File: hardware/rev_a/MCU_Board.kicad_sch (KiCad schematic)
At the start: 35 parts, among them J1 ST-Link, J2 Conn_01x08, J3 Bus, J4 Conn_01x08, J5 Conn_02x07_Odd_Even, SW1 nRST, U2 MC34063AD, U3 SN65HVD230, U5 STM32F042K6Tx, Y1 8Mhz

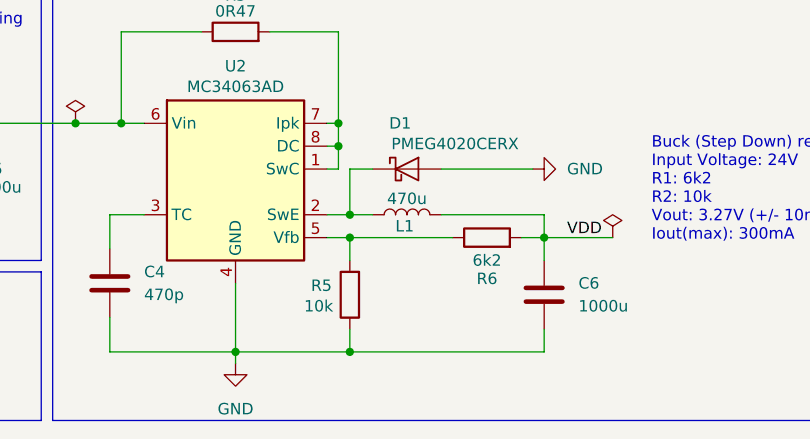
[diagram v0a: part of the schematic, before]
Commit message: Fix resistor value around DC/DC converter
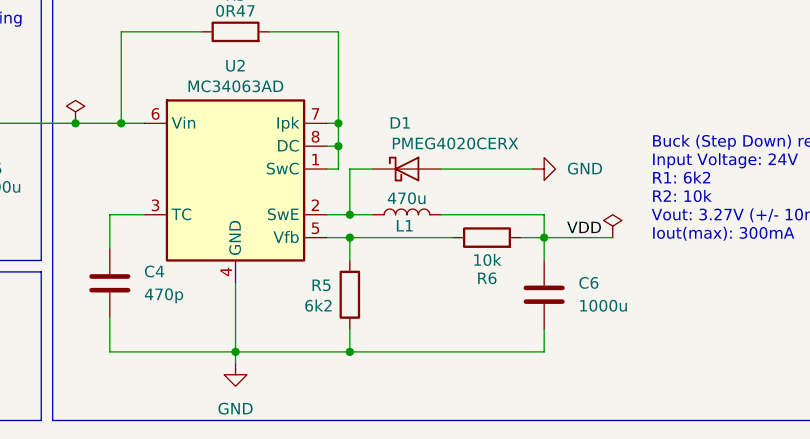
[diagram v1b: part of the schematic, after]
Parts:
- R5: value 10k -> 6k2
- R6: value 6k2 -> 10k
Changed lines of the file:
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@@
 			)
 		)
-		(property "Value" "10k"
+		(property "Value" "6k2"
 			(at 179.07 147.32 0)
 			(effects
@@
 			)
 		)
-		(property "Datasheet" "https://fr.farnell.com/multicomp/mcsr08x103-jtl/res-ceramique-10k-5-0-125w-0805/dp/2074340"
+		(property "Datasheet" "https://fr.farnell.com/multicomp/mcwr08x6201ftl/resistance-thick-film-6-2kohm/dp/2447709"
 			(at 184.15 146.05 0)
 			(effects
@@
 			)
 		)
-		(property "Value" "6k2"
+		(property "Value" "10k"
 			(at 199.39 142.24 90)
 			(effects
@@
 			)
 		)
-		(property "Datasheet" "https://fr.farnell.com/multicomp/mcwr08x6201ftl/resistance-thick-film-6-2kohm/dp/2447709"
+		(property "Datasheet" "https://fr.farnell.com/multicomp/mcsr08x103-jtl/res-ceramique-10k-5-0-125w-0805/dp/2074340"
 			(at 199.39 139.7 0)
 			(effects

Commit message: Version under review by PCBWay (Nucleo Shield)
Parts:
- removed C2: 18p, Capacitor_SMD:C_0805_2012Metric_Pad1.18x1.45mm_HandSolder, symbol Device:C
- removed C3, C7, C8, C9: 100n, Capacitor_SMD:C_0805_2012Metric_Pad1.18x1.45mm_HandSolder, symbol Device:C
- removed FB1: FerriteBead, Inductor_SMD:L_0805_2012Metric_Pad1.05x1.20mm_HandSolder, symbol Device:FerriteBead
- removed J1: ST-Link, custom:st-link, symbol Connector_Generic:Conn_01x04
- removed J2, J4: Conn_01x08, custom:CONN_01x08, symbol Connector_Generic:Conn_01x08
- removed J5: Conn_02x07_Odd_Even, custom:addr_jumpers, symbol Connector_Generic:Conn_02x07_Odd_Even
- removed R1: 100k, Resistor_SMD:R_0805_2012Metric_Pad1.20x1.40mm_HandSolder, symbol Device:R
- removed SW1: nRST, Button_Switch_SMD:SW_SPST_B3U-1000P-B, symbol Switch:SW_Push
- removed U5: STM32F042K6Tx, Package_QFP:LQFP-32_7x7mm_P0.8mm, symbol MCU_ST_STM32F0:STM32F042K6Tx
- removed Y1: 8Mhz, Crystal:Crystal_HC18-U_Vertical, symbol Device:Crystal_Small
- added J1, J5, J6, J7: Conn_01x15, Connector_PinHeader_2.54mm:PinHeader_1x15_P2.54mm_Vertical, symbol Connector_Generic:Conn_01x15
- added J2: Conn_01x02, Connector_PinHeader_2.54mm:PinHeader_1x02_P2.54mm_Vertical, symbol Connector_Generic:Conn_01x02
- C1: value 18p -> 100n; footprint Capacitor_SMD:C_0805_2012Metric_Pad1.18x1.45mm_HandSolder -> Capacitor_THT:C_Disc_D5.0mm_W2.5mm_P5.00mm
- C10: footprint Capacitor_SMD:C_0805_2012Metric_Pad1.18x1.45mm_HandSolder -> Capacitor_THT:C_Disc_D5.0mm_W2.5mm_P5.00mm
- C4: value 470p -> 680p; footprint Capacitor_SMD:C_0805_2012Metric_Pad1.18x1.45mm_HandSolder -> Capacitor_THT:C_Disc_D5.0mm_W2.5mm_P5.00mm
- R2, R4, R5, R6: footprint Resistor_SMD:R_0805_2012Metric_Pad1.20x1.40mm_HandSolder -> Resistor_THT:R_Axial_DIN0309_L9.0mm_D3.2mm_P2.54mm_Vertical
- R3: value 0R47 -> 0R33; footprint Resistor_SMD:R_0805_2012Metric_Pad1.20x1.40mm_HandSolder -> Resistor_THT:R_Axial_DIN0309_L9.0mm_D3.2mm_P2.54mm_Vertical
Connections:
- net GND: now also C1.1, J1.14 (Pin_14), J2.1 (Pin_1), J5.12 (Pin_12), J6.4 (Pin_4), J7.2 (Pin_2); no longer C1.2
- net at C5.1, D5.1 (K), D6.1 (A1)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: now also J2.2 (Pin_2)
- net CAN_RX renamed NUCLEO_PA11
- net NUCLEO_PA11: now also J5.3 (Pin_3), J6.13 (Pin_13)
- net CAN_TX renamed NUCLEO_PA12
- net NUCLEO_PA12: now also J5.11 (Pin_11), J6.5 (Pin_5)
- net VDD renamed NUCLEO_+3V3
- net NUCLEO_+3V3: now also C1.2, J1.2 (Pin_2), J7.14 (Pin_14)
- new net NUCLEO_+5V: J1.12 (Pin_12), J7.4 (Pin_4)
- new net NUCLEO_AREF: J1.3 (Pin_3), J7.13 (Pin_13)
- new net NUCLEO_NRST: J1.13 (Pin_13), J5.13 (Pin_13), J6.3 (Pin_3), J7.3 (Pin_3)
- new net NUCLEO_PA0: J1.4 (Pin_4), J7.12 (Pin_12)
- new net NUCLEO_PA1: J1.5 (Pin_5), J7.11 (Pin_11)
- new net NUCLEO_PA10: J5.14 (Pin_14), J6.2 (Pin_2)
- new net NUCLEO_PA2: J1.11 (Pin_11), J7.5 (Pin_5)
- new net NUCLEO_PA3: J1.6 (Pin_6), J7.10 (Pin_10)
- new net NUCLEO_PA4: J1.7 (Pin_7), J7.9 (Pin_9)
- new net NUCLEO_PA5: J1.8 (Pin_8), J7.8 (Pin_8)
- new net NUCLEO_PA6: J1.9 (Pin_9), J7.7 (Pin_7)
- new net NUCLEO_PA7: J1.10 (Pin_10), J7.6 (Pin_6)
- new net NUCLEO_PA8: J5.4 (Pin_4), J6.12 (Pin_12)
- new net NUCLEO_PA9: J5.15 (Pin_15), J6.1 (Pin_1)
- new net NUCLEO_PB0: J5.10 (Pin_10), J6.6 (Pin_6)
- new net NUCLEO_PB1: J5.7 (Pin_7), J6.9 (Pin_9)
- new net NUCLEO_PB3: J1.1 (Pin_1), J7.15 (Pin_15)
- new net NUCLEO_PB4: J5.1 (Pin_1), J6.15 (Pin_15)
- new net NUCLEO_PB5: J5.2 (Pin_2), J6.14 (Pin_14)
- new net NUCLEO_PB6: J5.8 (Pin_8), J6.8 (Pin_8)
- new net NUCLEO_PB7: J5.9 (Pin_9), J6.7 (Pin_7)
- new net NUCLEO_PC14: J5.6 (Pin_6), J6.10 (Pin_10)
- new net NUCLEO_PC15: J5.5 (Pin_5), J6.11 (Pin_11)
- new net NUCLEO_VIN: J1.15 (Pin_15), J7.1 (Pin_1)
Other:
- note added: "Buck (Step Down) regulation Input Voltage: 12V R1: 6k2 R2: 10k Vout: 3.27V (+/- 10mV) Iout(max): 450mA"
- note removed: "Buck (Step Down) regulation Input Voltage: 24V R1: 6k2 R2: 10k Vout: 3.27V (+/- 10mV) Iout(max): 300mA"
- moved on the sheet: C10, C4, C6, D1, D2, J3, JP1, L1, R2, R3, R4, R5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
